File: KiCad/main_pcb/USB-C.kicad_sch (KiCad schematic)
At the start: 13 parts, among them J4 1x1 Header, J5 1x1 Header, J6 USB-C, U2 CH340C, U3 JSMSEMI AMS1117-3.3V

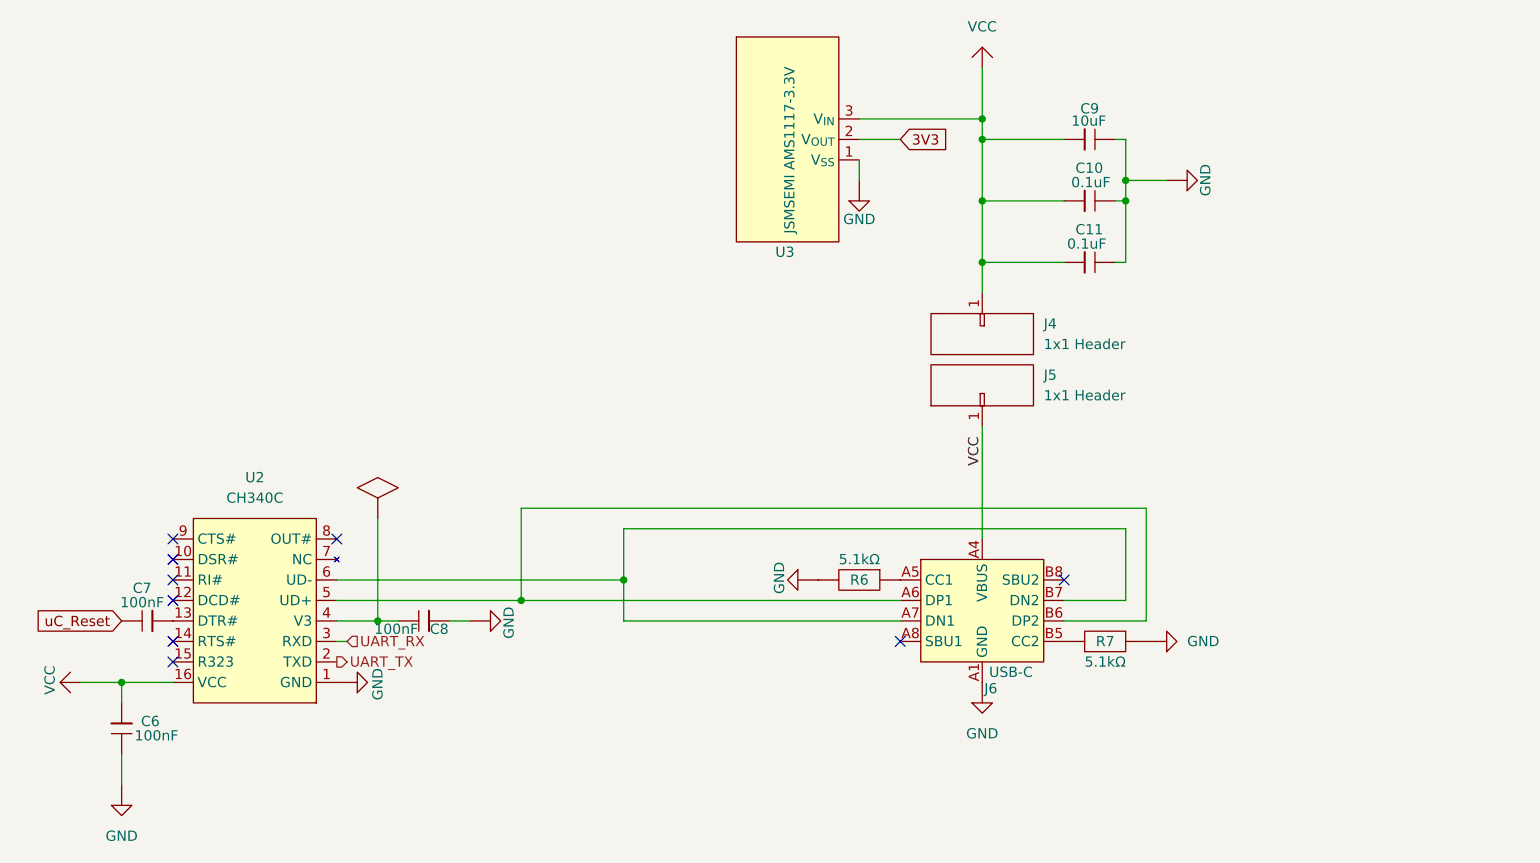
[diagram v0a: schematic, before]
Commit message: feat(schematic): Adds headers instead of direct screens plugging and refactors schematic.
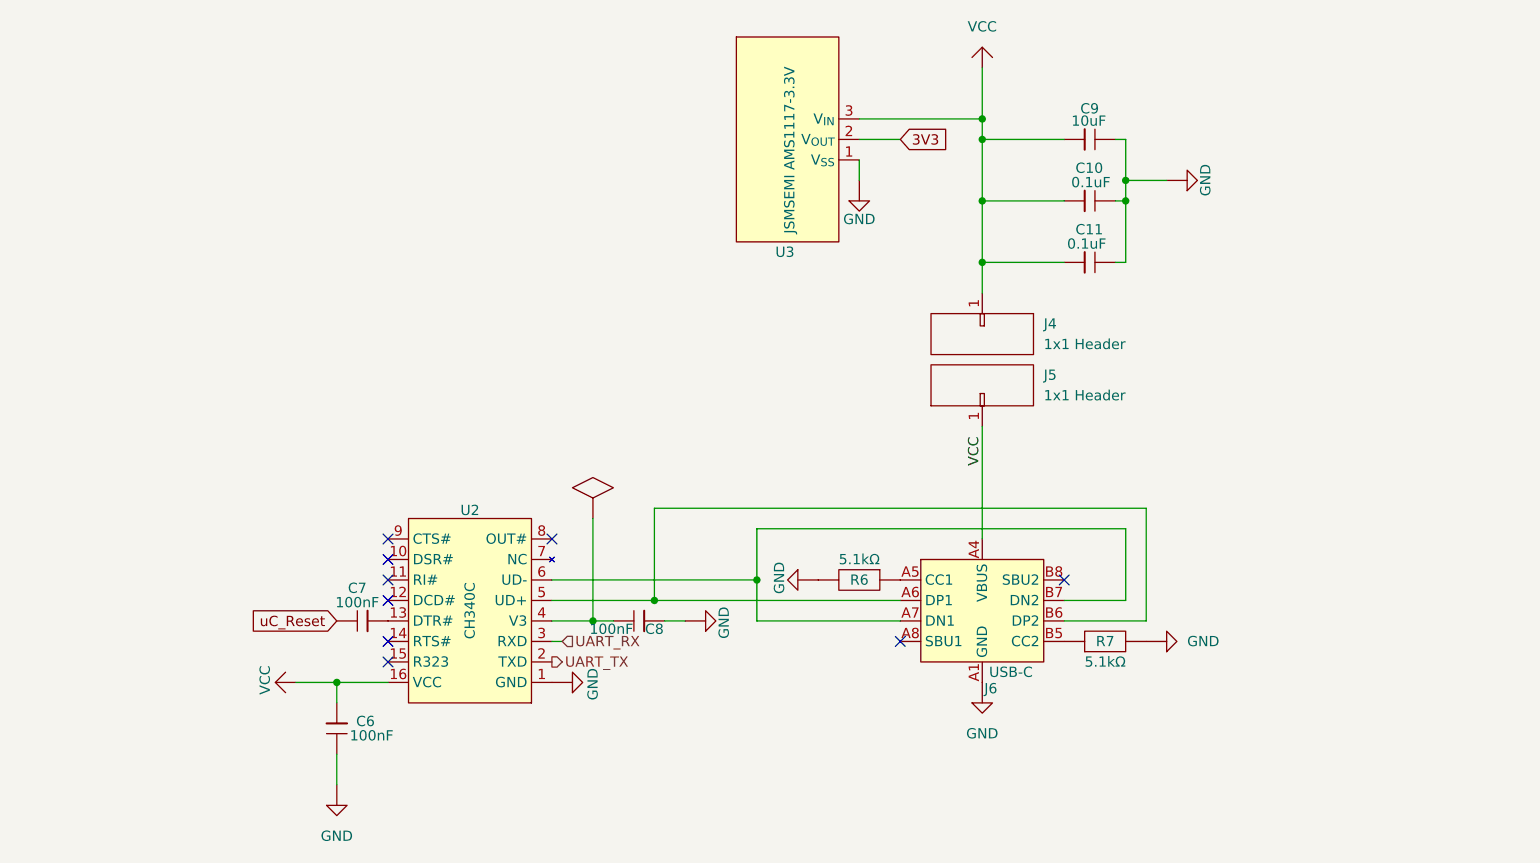
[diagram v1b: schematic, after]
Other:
- moved on the sheet: C6, C7, C8, U2

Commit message: Changes symbol and footprint for USB-C jack
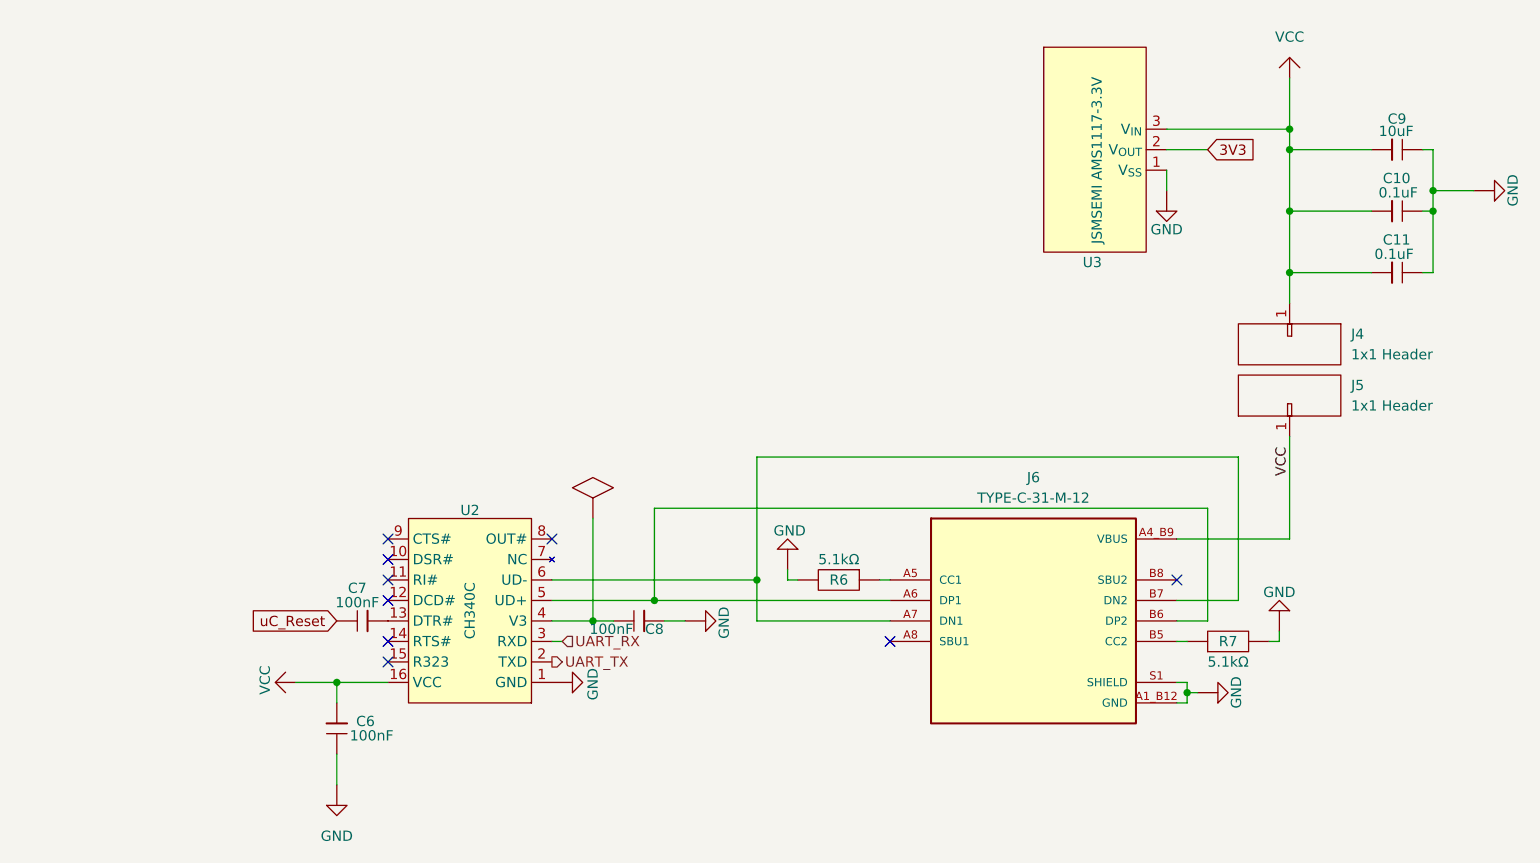
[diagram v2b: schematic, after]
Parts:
- removed J6: USB-C, Lilibrary:HRO_TYPE-C-31-M-12, symbol Lily's Pad:USB_TYPE-C-31-M-14
- added J6: TYPE-C-31-M-12, Lilibrary:HRO_TYPE-C-31-M-12, symbol Lily's Pad:TYPE-C-31-M-12
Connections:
- net GND: now also J6.A1_B12 (GND), J6.B1_A12 (GND), J6.S1 (SHIELD), J6.S2 (SHIELD), J6.S3 (SHIELD), J6.S4 (SHIELD)
- net VBUS: now also J6.A4_B9 (VBUS), J6.B4_A9 (VBUS)
- net at R6.1: now also J6.A5 (CC1)
- net at U2.5 (UD+): now also J6.A6 (DP1), J6.B6 (DP2)
- net at U2.6 (UD-): now also J6.A7 (DN1), J6.B7 (DN2)
- net at R7.1: now also J6.B5 (CC2)
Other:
- moved on the sheet: C10, C11, C9, J4, J5, R6, R7, U3

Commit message: feat(PCB): PCB first draft
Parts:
- C10, C11, C6, C7, C8, C9: footprint Capacitor_SMD:C_0201_0603Metric_Pad0.64x0.40mm_HandSolder -> Capacitor_SMD:C_0603_1608Metric_Pad1.08x0.95mm_HandSolder
- R6, R7: footprint Resistor_SMD:R_0201_0603Metric_Pad0.64x0.40mm_HandSolder -> Resistor_SMD:R_0603_1608Metric_Pad0.98x0.95mm_HandSolder
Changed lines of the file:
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@@
 			)
 		)
-		(property "Footprint" "Capacitor_SMD:C_0201_0603Metric_Pad0.64x0.40mm_HandSolder"
+		(property "Footprint" "Capacitor_SMD:C_0603_1608Metric_Pad1.08x0.95mm_HandSolder"
 			(at 220.98 49.53 0)
 			(effects
@@
 			)
 		)
-		(property "Footprint" "Capacitor_SMD:C_0201_0603Metric_Pad0.64x0.40mm_HandSolder"
+		(property "Footprint" "Capacitor_SMD:C_0603_1608Metric_Pad1.08x0.95mm_HandSolder"
 			(at 91.44 107.95 0)
 			(effects
@@
 			)
 		)
-		(property "Footprint" "Resistor_SMD:R_0201_0603Metric_Pad0.64x0.40mm_HandSolder"
+		(property "Footprint" "Resistor_SMD:R_0603_1608Metric_Pad0.98x0.95mm_HandSolder"
 			(at 199.39 110.49 0)
 			(effects
@@
 			)
 		)
-		(property "Footprint" "Capacitor_SMD:C_0201_0603Metric_Pad0.64x0.40mm_HandSolder"
+		(property "Footprint" "Capacitor_SMD:C_0603_1608Metric_Pad1.08x0.95mm_HandSolder"
 			(at 125.73 107.95 0)
 			(effects
@@
 			)
 		)
-		(property "Footprint" "Capacitor_SMD:C_0201_0603Metric_Pad0.64x0.40mm_HandSolder"
+		(property "Footprint" "Capacitor_SMD:C_0603_1608Metric_Pad1.08x0.95mm_HandSolder"
 			(at 88.9 121.92 0)
 			(effects
@@
 			)
 		)
-		(property "Footprint" "Capacitor_SMD:C_0201_0603Metric_Pad0.64x0.40mm_HandSolder"
+		(property "Footprint" "Capacitor_SMD:C_0603_1608Metric_Pad1.08x0.95mm_HandSolder"
 			(at 220.98 64.77 0)
 			(effects
@@
 			)
 		)
-		(property "Footprint" "Capacitor_SMD:C_0201_0603Metric_Pad0.64x0.40mm_HandSolder"
+		(property "Footprint" "Capacitor_SMD:C_0603_1608Metric_Pad1.08x0.95mm_HandSolder"
 			(at 220.98 57.15 0)
 			(effects
@@
 			)
 		)
-		(property "Footprint" "Resistor_SMD:R_0201_0603Metric_Pad0.64x0.40mm_HandSolder"
+		(property "Footprint" "Resistor_SMD:R_0603_1608Metric_Pad0.98x0.95mm_HandSolder"
 			(at 151.13 102.87 0)
 			(effects
